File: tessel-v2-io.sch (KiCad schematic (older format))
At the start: 0 parts

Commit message: readding io
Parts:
- added C? (x2): 8pF, symbol C
- added C?: 10uF, symbol C
- added C? (x4): 0.1uF, symbol C
- added D? (x4): Green, symbol LED
- added J? (x2): MODULE_HEADER, symbol MODULE_HEADER
- added P? (x3): CONN_01X02, symbol CONN_01X02
- added P?: CONN_01X07, symbol CONN_01X07
- added P?: CONN_02X02, symbol CONN_02X02
- added P? (x2): CONN_02X01, symbol CONN_02X01
- added P? (x2): USB_A_2_stack, symbol USB_A_2_stack
- added P?: RJ45_LEDs, symbol RJ45_LEDs
- added P?: CONN_01X01, symbol CONN_01X01
- added R?: 8.2kR, symbol R
- added R?: 10kR, symbol R
- added R?: 649R, symbol R
- added R? (x3): 4.7kR, symbol R
- added R? (x6): R, 300R, symbol R
- added R?: 6.19kR, 1%, symbol R
- added U? (x3): MT7620N, symbol MT7620N
- added U?: CY7C65632, symbol CY7C65632
- added X?: 12MHz, symbol CRYSTAL
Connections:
- net labels added: +3V3, +5V, GND, L2_yellow, L4_green, M1_CLK, M1_G1/TX, M1_G2/RX, M1_G3, M1_MISO, M1_MOSI, M1_SCL, M1_SDA, M2_CLK, M2_G1/TX, M2_G2/RX, M2_G3, M2_MISO, M2_MOSI, M2_SCL, M2_SDA, MT_CLK, MT_CS0, MT_CS1, MT_GPIO0, MT_HOLD, MT_MISO, MT_MOSI, MT_RX, MT_SCL, MT_SDA, MT_TX, MT_WP, UPHY0_PADM, UPHY0_PADP, UPHY0_VRES, USB_DD+[1], USB_DD+[2], USB_DD+[3], USB_DD-[1], USB_DD-[2], USB_DD-[3], USB_GANG, USB_GREEN1, USB_GREEN2, USB_GREEN3, USB_GREEN4, USB_RESET#, USB_RREF, USB_SEL27, USB_SEL48, USB_XTAL_IN, USB_XTAL_OUT
- wire segments 0 -> 192
- no-connect marks 0 -> 6
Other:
- note added: "externally regulated to 3.3v"

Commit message: io pins, jtag, cortex, high level pins
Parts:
- added D?: TVS-2, symbol TVS-2
- added J? (x2): CONN_02X05, symbol CONN_02X05
- added J?: USB-MICRO-B, symbol USB-MICRO-B
- added R?: 10kR, symbol R
- R?: value 8.2kR -> 8.2kR, 1%
- R?: value 649R -> 649R, 1%
- R? (x6): value R -> 300R; footprint 300R -> 0402
- gave numbers to parts that had none: 1
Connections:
- net labels added: +3.3V, 3.3V_CP, 3.3V_PORTA, 3.3V_PORTB, MT_RTCH, MT_TCLK, MT_TDI, MT_TDO, MT_TWS, MT_~RESET, PORTA_CLK, PORTA_G1/TX, PORTA_G2/RX, PORTA_G3, PORTA_MISO, PORTA_MOSI, PORTA_SCL, PORTA_SDA, PORTB_CLK, PORTB_G1/TX, PORTB_G2/RX, PORTB_G3, PORTB_MISO, PORTB_MOSI, PORTB_SCL, PORTB_SDA, SAM_USBDM, SAM_USBDP, SAM_USB_DM, SAM_USB_DP, SAM_USB_SHELL, SAM_~RESET, SWCLK, SWDIO, USB_DD+[4], USB_DD-[4]
- net labels removed: +3V3, M1_CLK, M1_G1/TX, M1_G2/RX, M1_G3, M1_MISO, M1_MOSI, M1_SCL, M1_SDA, M2_CLK, M2_G1/TX, M2_G2/RX, M2_G3, M2_MISO, M2_MOSI, M2_SCL, M2_SDA
- wire segments 192 -> 291
- no-connect marks 6 -> 10
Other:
- note added: "1%"
- moved on the sheet: D?, J?, R?

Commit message: wiring up more i/o to cp
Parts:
- removed J?: CONN_02X02, symbol CONN_02X02
- added C? (x2): 0.1uF, symbol C
- added C? (x2): 10uF, symbol C
- added D? (x4): TVS-2, symbol TVS-2
- added L? (x2): BLM21PG221SN1D, symbol INDUCTOR
- added R?: 4.7kR, symbol R
- C? (x2): value 8pF -> 20pF
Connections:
- net MT_TDI is gone; now on net MT_EPHY_LED1: J?.8 (P8)
- net MT_TWS is gone; now on net MT_EPHY_LED2: J?.2 (P2)
- net +3.3V: now also R?.1
- net +5V: now also C?.2, C?.2, L?.2, L?.2
- net GND: now also C?.1, C?.1, C?.1, C?.1, D?.3, D?.3, D?.3, D?.3
- net MT_TCLK: now also U?.7 (EPHY_LED3_N_JTCLK)
- net MT_TDO: now also R?.1, U?.82 (EPHY_LED0_N_JTDO)
- net MT_~RESET: now also U?.9 (EPHY_LED4_N_JTRST_N)
- net USB_DD+[1]: now also D?.1
- net USB_DD+[3]: now also D?.1
- net USB_DD+[4]: now also D?.1
- net USB_DD-[1]: now also D?.2
- net USB_DD-[3]: now also D?.2
- net USB_DD-[4]: now also D?.2
- net USB_SEL27: now also R?.2
- net USB_SEL48: now also R?.2
- net MT_EPHY_LED1: now reaches U?.8 (EPHY_LED1_N_JTDI)
- net MT_EPHY_LED2: now reaches U?.83 (EPHY_LED2_N_JTMS)
- net at J?.7 (D+[2]), U?.10 (DD+[2]): now also D?.1
- net at J?.6 (D-[2]), U?.9 (DD-[2]): now also D?.2
- new net: C?.2, L?.1 (x2)
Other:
- moved on the sheet: J?, R?

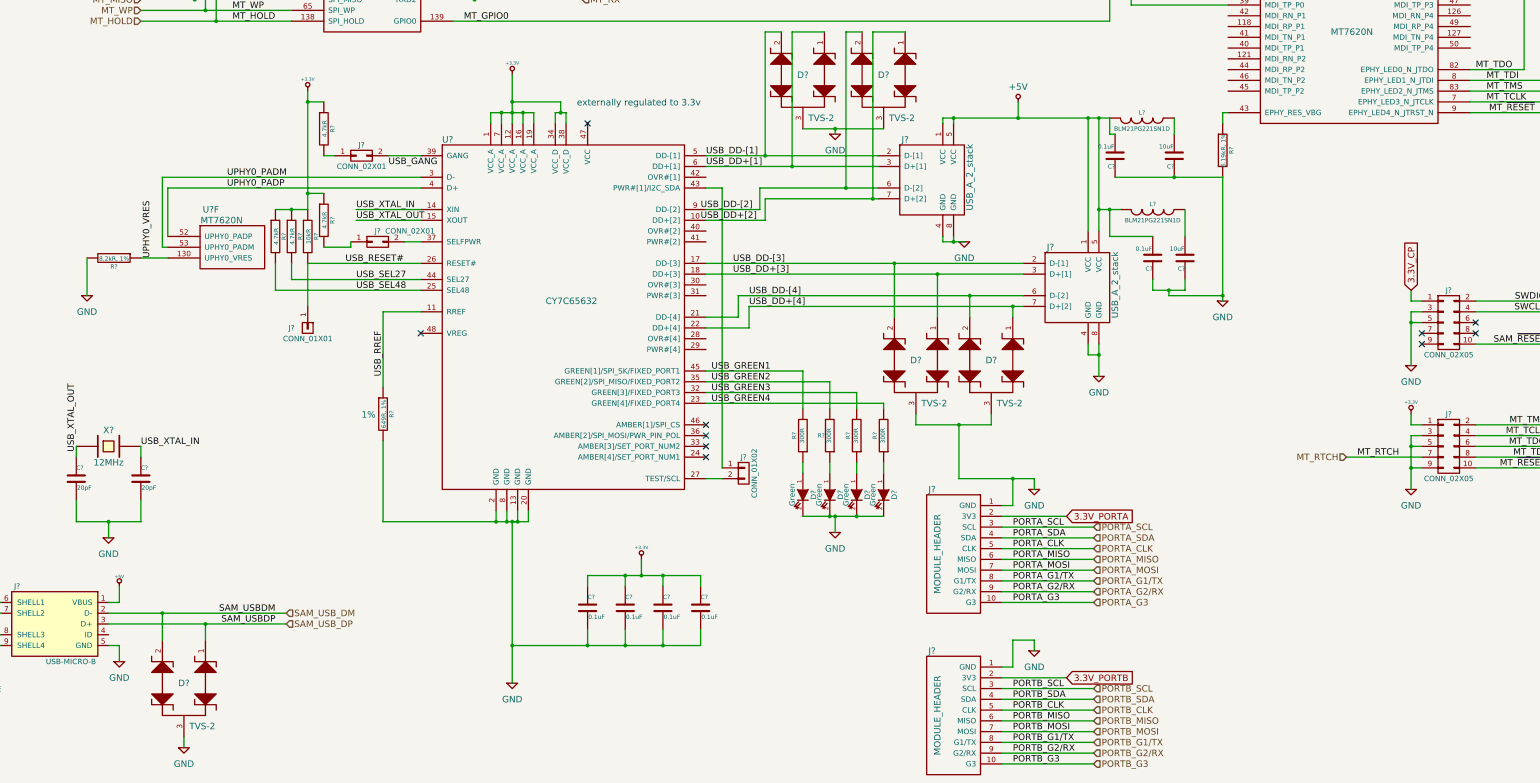
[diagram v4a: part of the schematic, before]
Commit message: added power reg to downstream usb
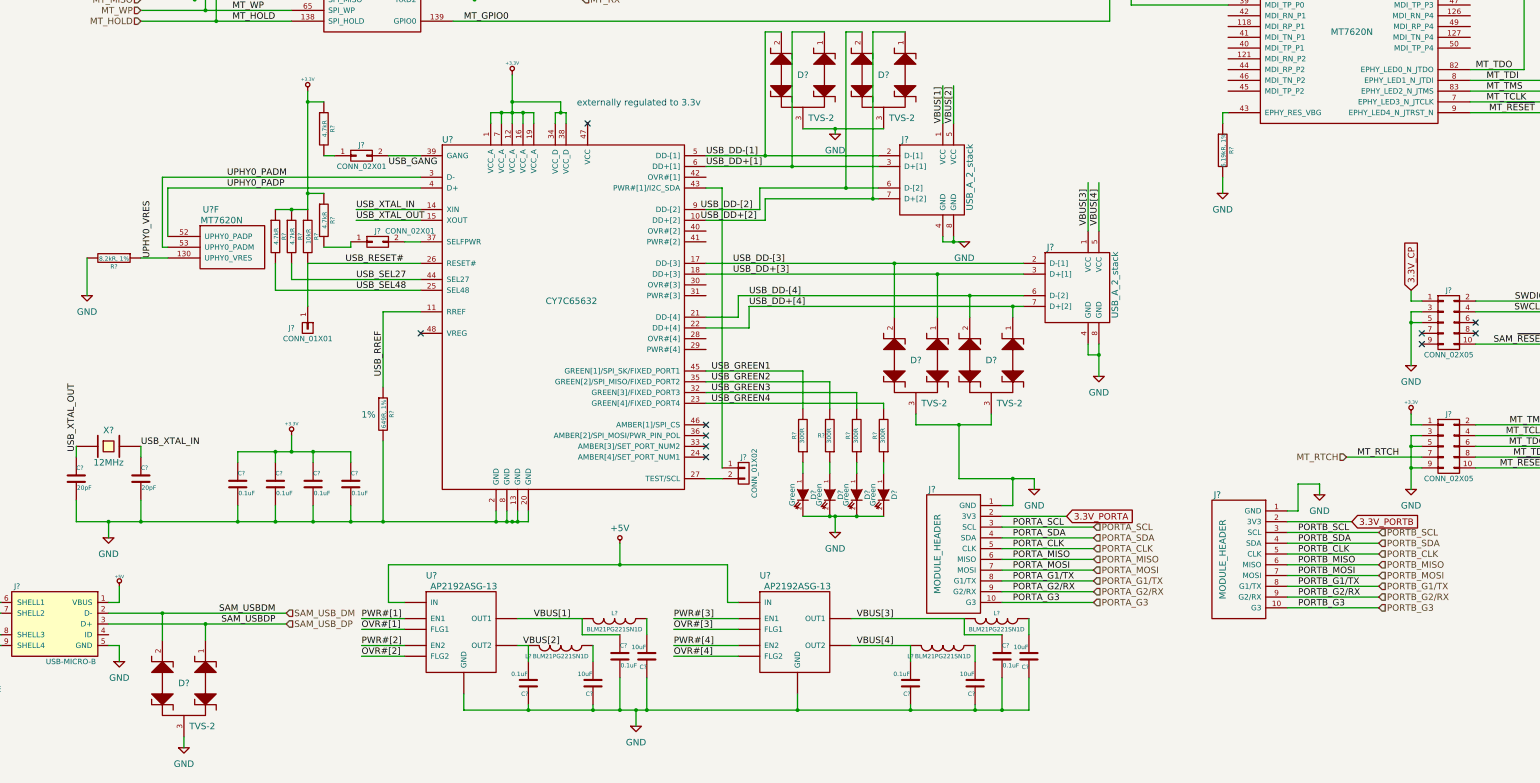
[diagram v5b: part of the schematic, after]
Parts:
- removed C?: 0.1uF, symbol C
- removed C?: 10uF, symbol C
- removed L?: BLM21PG221SN1D, symbol INDUCTOR
- added C? (x3): 0.1uF, symbol C
- added C? (x3): 10uF, symbol C
- added L? (x3): BLM21PG221SN1D, symbol INDUCTOR
- added U? (x2): AP2192ASG-13, symbol AP2192ASG-13
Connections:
- net labels added: OVR#[1], OVR#[2], OVR#[3], OVR#[4], PWR#[1], PWR#[2], PWR#[3], PWR#[4], VBUS[1], VBUS[2], VBUS[3], VBUS[4]
- wire segments 269 -> 290
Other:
- moved on the sheet: C?, J?, L?

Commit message: labeling final nets
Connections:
- net labels added: USB_SCL
- wire segments 290 -> 369
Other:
- moved on the sheet: J?

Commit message: annotated
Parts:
- gave numbers to parts that had none: 63

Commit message: give nF some love
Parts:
- C703, C704, C705, C706, C707, C709, C711, C713: value 0.1uF -> 100nF
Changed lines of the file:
@@
 P 3350 7550
 F 0 "C703" H 3350 7650 40  0000 L CNN
-F 1 "0.1uF" H 3356 7465 40  0000 L CNN
+F 1 "100nF" H 3356 7465 40  0000 L CNN
 F 2 "" H 3388 7400 30  0000 C CNN
 F 3 "" H 3350 7550 60  0000 C CNN
@@
 P 3700 7550
 F 0 "C704" H 3700 7650 40  0000 L CNN
-F 1 "0.1uF" H 3706 7465 40  0000 L CNN
+F 1 "100nF" H 3706 7465 40  0000 L CNN
 F 2 "" H 3738 7400 30  0000 C CNN
 F 3 "" H 3700 7550 60  0000 C CNN
@@
 P 4050 7550
 F 0 "C705" H 4050 7650 40  0000 L CNN
-F 1 "0.1uF" H 4056 7465 40  0000 L CNN
+F 1 "100nF" H 4056 7465 40  0000 L CNN
 F 2 "" H 4088 7400 30  0000 C CNN
 F 3 "" H 4050 7550 60  0000 C CNN
@@
 P 4400 7550
 F 0 "C706" H 4400 7650 40  0000 L CNN
-F 1 "0.1uF" H 4406 7465 40  0000 L CNN
+F 1 "100nF" H 4406 7465 40  0000 L CNN
 F 2 "" H 4438 7400 30  0000 C CNN
 F 3 "" H 4400 7550 60  0000 C CNN
@@
 P 6900 9150
 F 0 "C709" H 6900 9250 40  0000 L CNN
-F 1 "0.1uF" H 6906 9065 40  0000 L CNN
+F 1 "100nF" H 6906 9065 40  0000 L CNN
 F 2 "" H 6938 9000 30  0000 C CNN
 F 3 "" H 6900 9150 60  0000 C CNN
@@
 P 6050 9400
 F 0 "C707" H 6050 9500 40  0000 L CNN
-F 1 "0.1uF" H 6056 9315 40  0000 L CNN
+F 1 "100nF" H 6056 9315 40  0000 L CNN
 F 2 "" H 6088 9250 30  0000 C CNN
 F 3 "" H 6050 9400 60  0000 C CNN
@@
 P 10450 9150
 F 0 "C713" H 10450 9250 40  0000 L CNN
-F 1 "0.1uF" H 10456 9065 40  0000 L CNN
+F 1 "100nF" H 10456 9065 40  0000 L CNN
 F 2 "" H 10488 9000 30  0000 C CNN
 F 3 "" H 10450 9150 60  0000 C CNN
@@
 P 9600 9400
 F 0 "C711" H 9600 9500 40  0000 L CNN
-F 1 "0.1uF" H 9606 9315 40  0000 L CNN
+F 1 "100nF" H 9606 9315 40  0000 L CNN
 F 2 "" H 9638 9250 30  0000 C CNN
 F 3 "" H 9600 9400 60  0000 C CNN
